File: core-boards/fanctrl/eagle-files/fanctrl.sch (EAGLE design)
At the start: 30 parts, among them J1 3-PIN_2MM-H, U1 MCP9701T-E/TT

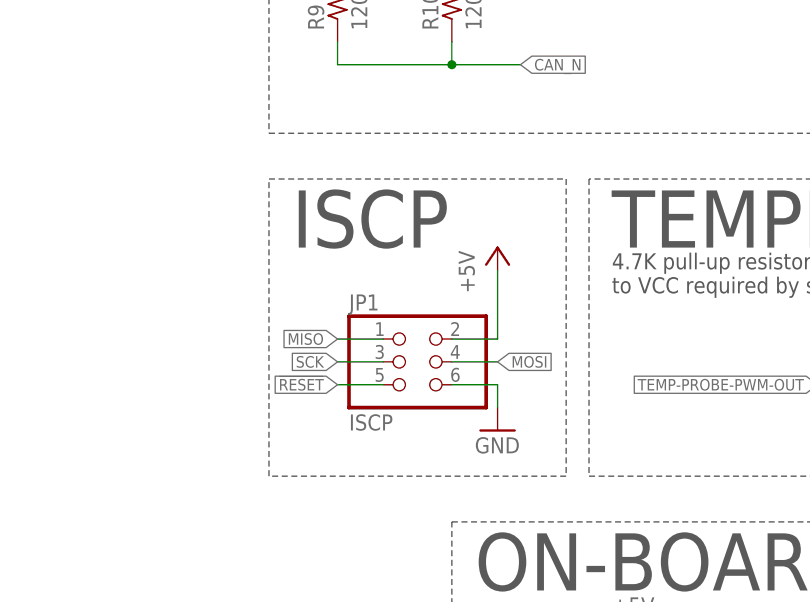
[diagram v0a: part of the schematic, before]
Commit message: Fix typo: ISCP --> ICSP.
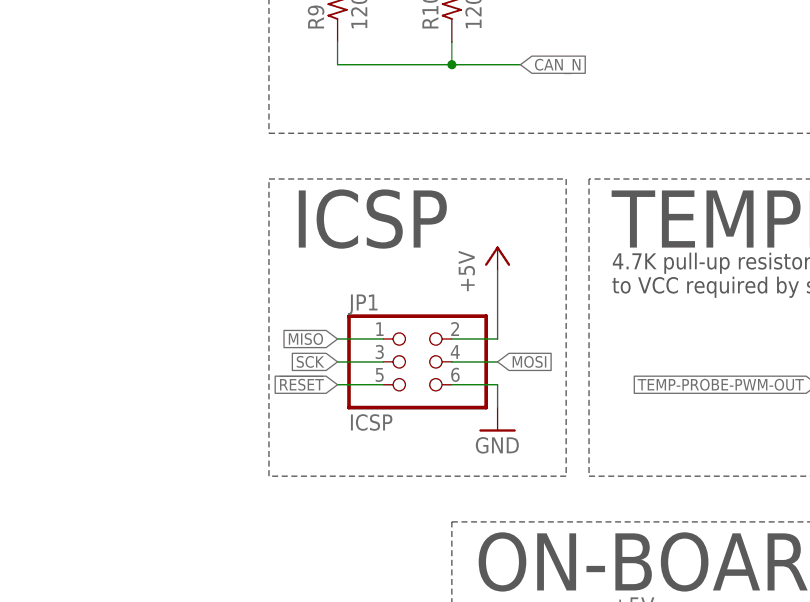
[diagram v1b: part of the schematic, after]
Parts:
- JP1: value ISCP -> ICSP
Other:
- note added: "ICSP"
- note removed: "ISCP"
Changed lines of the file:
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@@
 <part name="R9" library="rcl" library_urn="urn:adsk.eagle:library:334" deviceset="R-US_" device="R0603" package3d_urn="urn:adsk.eagle:package:23555/3" value="120Ω"/>
 <part name="R10" library="rcl" library_urn="urn:adsk.eagle:library:334" deviceset="R-US_" device="R0603" package3d_urn="urn:adsk.eagle:package:23555/3" value="120Ω"/>
-<part name="JP1" library="pinhead" library_urn="urn:adsk.eagle:library:325" deviceset="PINHD-2X3" device="" package3d_urn="urn:adsk.eagle:package:22462/2" value="ISCP"/>
+<part name="JP1" library="pinhead" library_urn="urn:adsk.eagle:library:325" deviceset="PINHD-2X3" device="" package3d_urn="urn:adsk.eagle:package:22462/2" value="ICSP"/>
 <part name="P+10" library="supply1" library_urn="urn:adsk.eagle:library:371" deviceset="+5V" device=""/>
 <part name="GND17" library="supply1" library_urn="urn:adsk.eagle:library:371" deviceset="GND" device=""/>
@@
 <wire x1="187.96" y1="129.54" x2="187.96" y2="96.52" width="0.1524" layer="97" style="shortdash"/>
 <wire x1="187.96" y1="96.52" x2="154.94" y2="96.52" width="0.1524" layer="97" style="shortdash"/>
-<text x="157.48" y="121.92" size="6.35" layer="97" font="vector" ratio="12">ISCP</text>
+<text x="157.48" y="121.92" size="6.35" layer="97" font="vector" ratio="12">ICSP</text>
 <text x="10.16" y="111.76" size="1.778" layer="97">IN = Write to the fan</text>
 <text x="10.16" y="109.22" size="1.778" layer="97">OUT = Read from the fan</text>

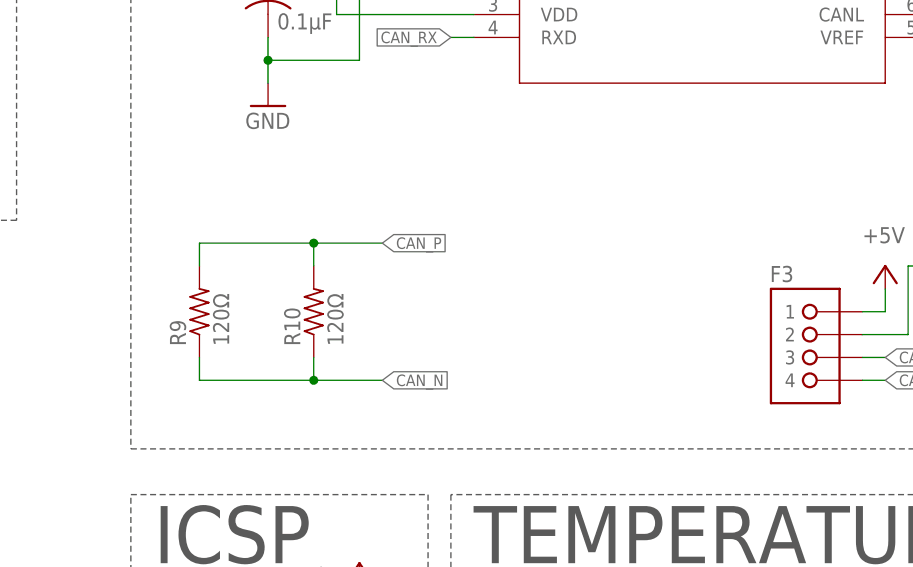
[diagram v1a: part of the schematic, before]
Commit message: Jank jumper for CAN resistor added.
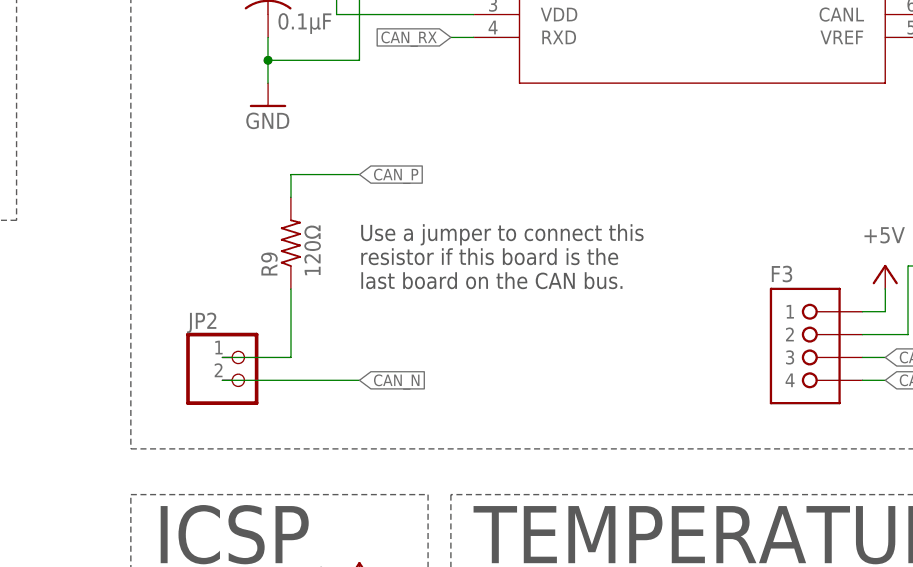
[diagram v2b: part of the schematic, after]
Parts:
- removed R10: 120Ω, rcl:R-US_R0603
- added JP2: (no value), pinhead:PINHD-1X2
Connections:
- new net N$1: JP2.1, R9.1
- net CAN_N: now also JP2.2; no longer R10.1, R9.1
- net CAN_P: no longer R10.2
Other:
- note added: "Use a jumper to connect this resistor if this board is the last board on the CAN bus."
- moved on the sheet: R9
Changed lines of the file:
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@@
 <part name="R8" library="rcl" library_urn="urn:adsk.eagle:library:334" deviceset="R-US_" device="R0603" package3d_urn="urn:adsk.eagle:package:23555/3" value="4.7K"/>
 <part name="R9" library="rcl" library_urn="urn:adsk.eagle:library:334" deviceset="R-US_" device="R0603" package3d_urn="urn:adsk.eagle:package:23555/3" value="120Ω"/>
-<part name="R10" library="rcl" library_urn="urn:adsk.eagle:library:334" deviceset="R-US_" device="R0603" package3d_urn="urn:adsk.eagle:package:23555/3" value="120Ω"/>
 <part name="JP1" library="pinhead" library_urn="urn:adsk.eagle:library:325" deviceset="PINHD-2X3" device="" package3d_urn="urn:adsk.eagle:package:22462/2" value="ICSP"/>
 <part name="P+10" library="supply1" library_urn="urn:adsk.eagle:library:371" deviceset="+5V" device=""/>
@@
 <part name="F3" library="RoboJackets-Connectors" deviceset="4-PIN_2MM-*" device="H"/>
 <part name="J1" library="RoboJackets-Connectors" deviceset="3-PIN_2MM-*" device="H"/>
+<part name="JP2" library="pinhead" library_urn="urn:adsk.eagle:library:325" deviceset="PINHD-1X2" device="" package3d_urn="urn:adsk.eagle:package:22435/2">
+<attribute name="SPICEPREFIX" value="B"/>
+</part>
 </parts>
 <sheets>
@@
 <text x="10.16" y="111.76" size="1.778" layer="97">IN = Write to the fan</text>
 <text x="10.16" y="109.22" size="1.778" layer="97">OUT = Read from the fan</text>
+<text x="180.34" y="152.4" size="1.778" layer="97" font="vector">Use a jumper to connect this
+resistor if this board is the
+last board on the CAN bus. </text>
 </plain>
 <instances>
@@
 <attribute name="VALUE" x="227.33" y="108.458" size="1.778" layer="96"/>
 </instance>
-<instance part="R9" gate="G$1" x="162.56" y="149.86" smashed="yes" rot="R90">
-<attribute name="NAME" x="161.0614" y="146.05" size="1.778" layer="95" rot="R90"/>
-<attribute name="VALUE" x="165.862" y="146.05" size="1.778" layer="96" rot="R90"/>
-</instance>
-<instance part="R10" gate="G$1" x="175.26" y="149.86" smashed="yes" rot="R90">
-<attribute name="NAME" x="173.7614" y="146.05" size="1.778" layer="95" rot="R90"/>
-<attribute name="VALUE" x="178.562" y="146.05" size="1.778" layer="96" rot="R90"/>
+<instance part="R9" gate="G$1" x="172.72" y="157.48" smashed="yes" rot="R90">
+<attribute name="NAME" x="171.2214" y="153.67" size="1.778" layer="95" rot="R90"/>
+<attribute name="VALUE" x="176.022" y="153.67" size="1.778" layer="96" rot="R90"/>
 </instance>
 <instance part="JP1" gate="A" x="170.18" y="109.22" smashed="yes">
@@
 <attribute name="NAME" x="248.92" y="119.38" size="1.778" layer="95" font="vector" align="top-left"/>
 <attribute name="VALUE" x="248.92" y="99.06" size="1.778" layer="96" font="vector"/>
+</instance>
+<instance part="JP2" gate="G$1" x="167.64" y="142.24" smashed="yes">
+<attribute name="NAME" x="161.29" y="147.955" size="1.778" layer="95"/>
+<attribute name="VALUE" x="161.29" y="137.16" size="1.778" layer="96"/>
 </instance>
 </instances>
@@
 </segment>
 <segment>
-<pinref part="R10" gate="G$1" pin="2"/>
-<label x="182.88" y="157.48" size="1.27" layer="95" font="vector" xref="yes"/>
+<wire x1="172.72" y1="165.1" x2="180.34" y2="165.1" width="0.1524" layer="91"/>
+<label x="180.34" y="165.1" size="1.27" layer="95" font="vector" xref="yes"/>
 <pinref part="R9" gate="G$1" pin="2"/>
-<wire x1="162.56" y1="154.94" x2="162.56" y2="157.48" width="0.1524" layer="91"/>
-<wire x1="162.56" y1="157.48" x2="175.26" y2="157.48" width="0.1524" layer="91"/>
-<wire x1="175.26" y1="157.48" x2="175.26" y2="154.94" width="0.1524" layer="91"/>
-<wire x1="175.26" y1="157.48" x2="182.88" y2="157.48" width="0.1524" layer="91"/>
-<junction x="175.26" y="157.48"/>
+<wire x1="172.72" y1="165.1" x2="172.72" y2="162.56" width="0.1524" layer="91"/>
 </segment>
 </net>
@@
 </segment>
 <segment>
-<pinref part="R10" gate="G$1" pin="1"/>
-<label x="182.88" y="142.24" size="1.27" layer="95" font="vector" xref="yes"/>
-<pinref part="R9" gate="G$1" pin="1"/>
-<wire x1="162.56" y1="144.78" x2="162.56" y2="142.24" width="0.1524" layer="91"/>
-<wire x1="162.56" y1="142.24" x2="175.26" y2="142.24" width="0.1524" layer="91"/>
-<wire x1="175.26" y1="142.24" x2="182.88" y2="142.24" width="0.1524" layer="91"/>
-<wire x1="175.26" y1="144.78" x2="175.26" y2="142.24" width="0.1524" layer="91"/>
-<junction x="175.26" y="142.24"/>
+<pinref part="JP2" gate="G$1" pin="2"/>
+<wire x1="165.1" y1="142.24" x2="180.34" y2="142.24" width="0.1524" layer="91"/>
+<label x="180.34" y="142.24" size="1.27" layer="95" font="vector" xref="yes"/>
 </segment>
 </net>
@@
 </segment>
 </net>
+<net name="N$1" class="0">
+<segment>
+<pinref part="JP2" gate="G$1" pin="1"/>
+<wire x1="165.1" y1="144.78" x2="172.72" y2="144.78" width="0.1524" layer="91"/>
+<pinref part="R9" gate="G$1" pin="1"/>
+<wire x1="172.72" y1="144.78" x2="172.72" y2="152.4" width="0.1524" layer="91"/>
+</segment>
+</net>

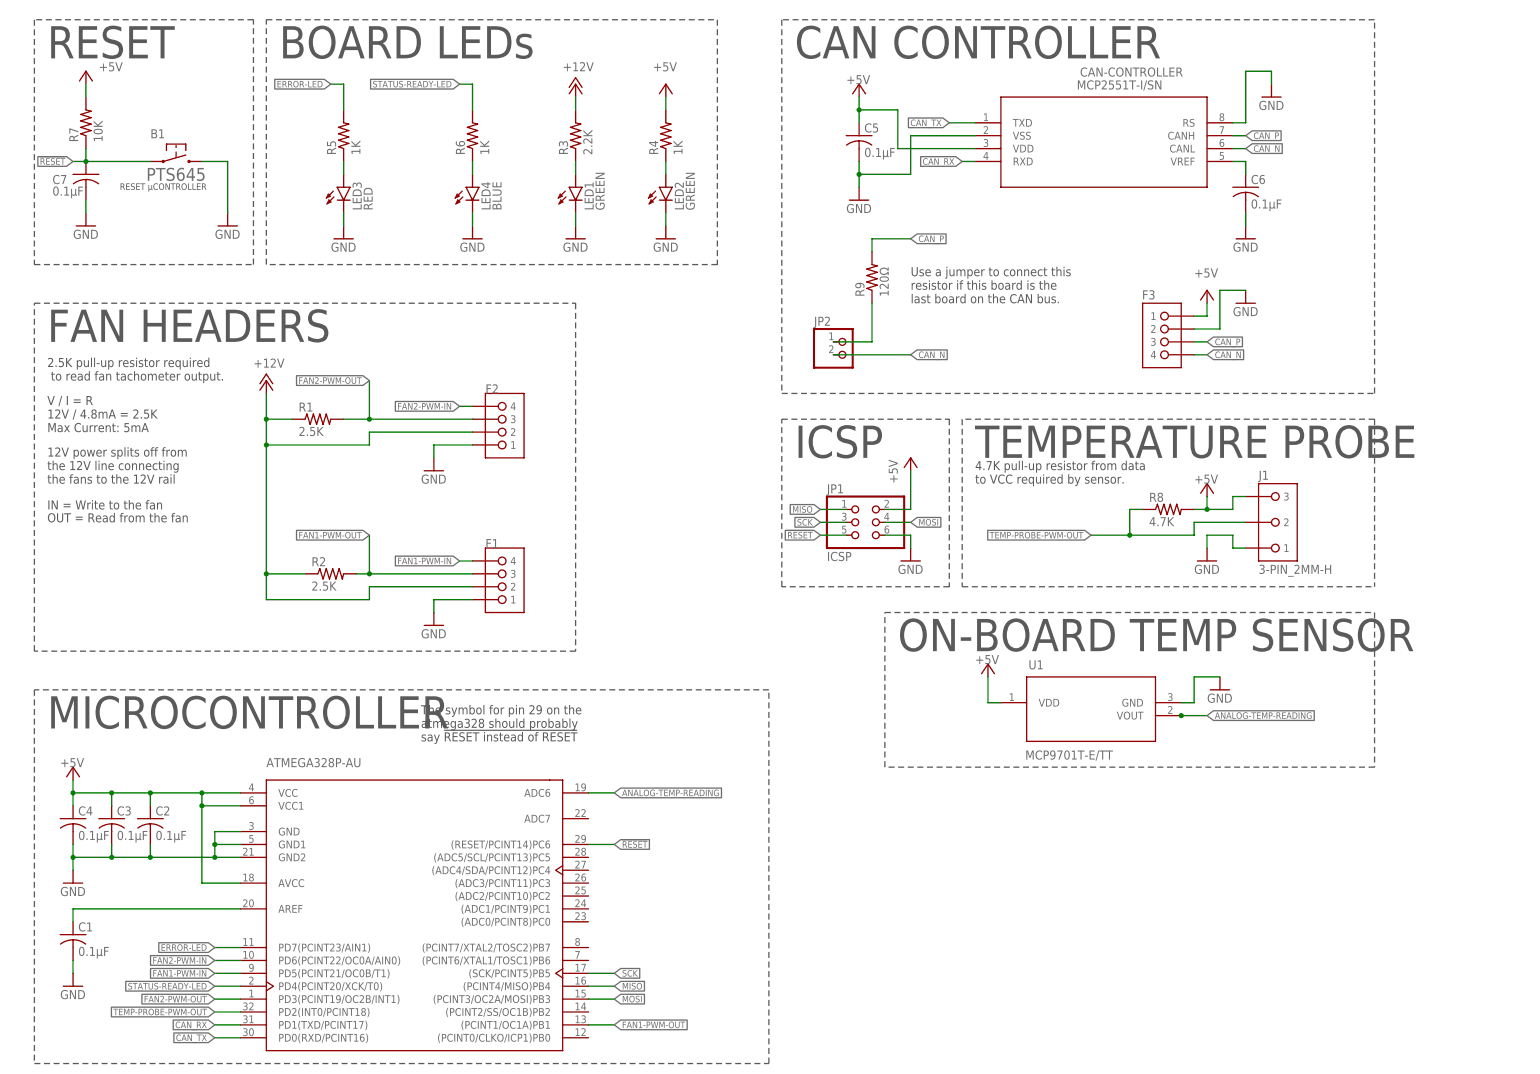
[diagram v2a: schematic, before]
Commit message: Fix LED Resist. values --> 470ohm
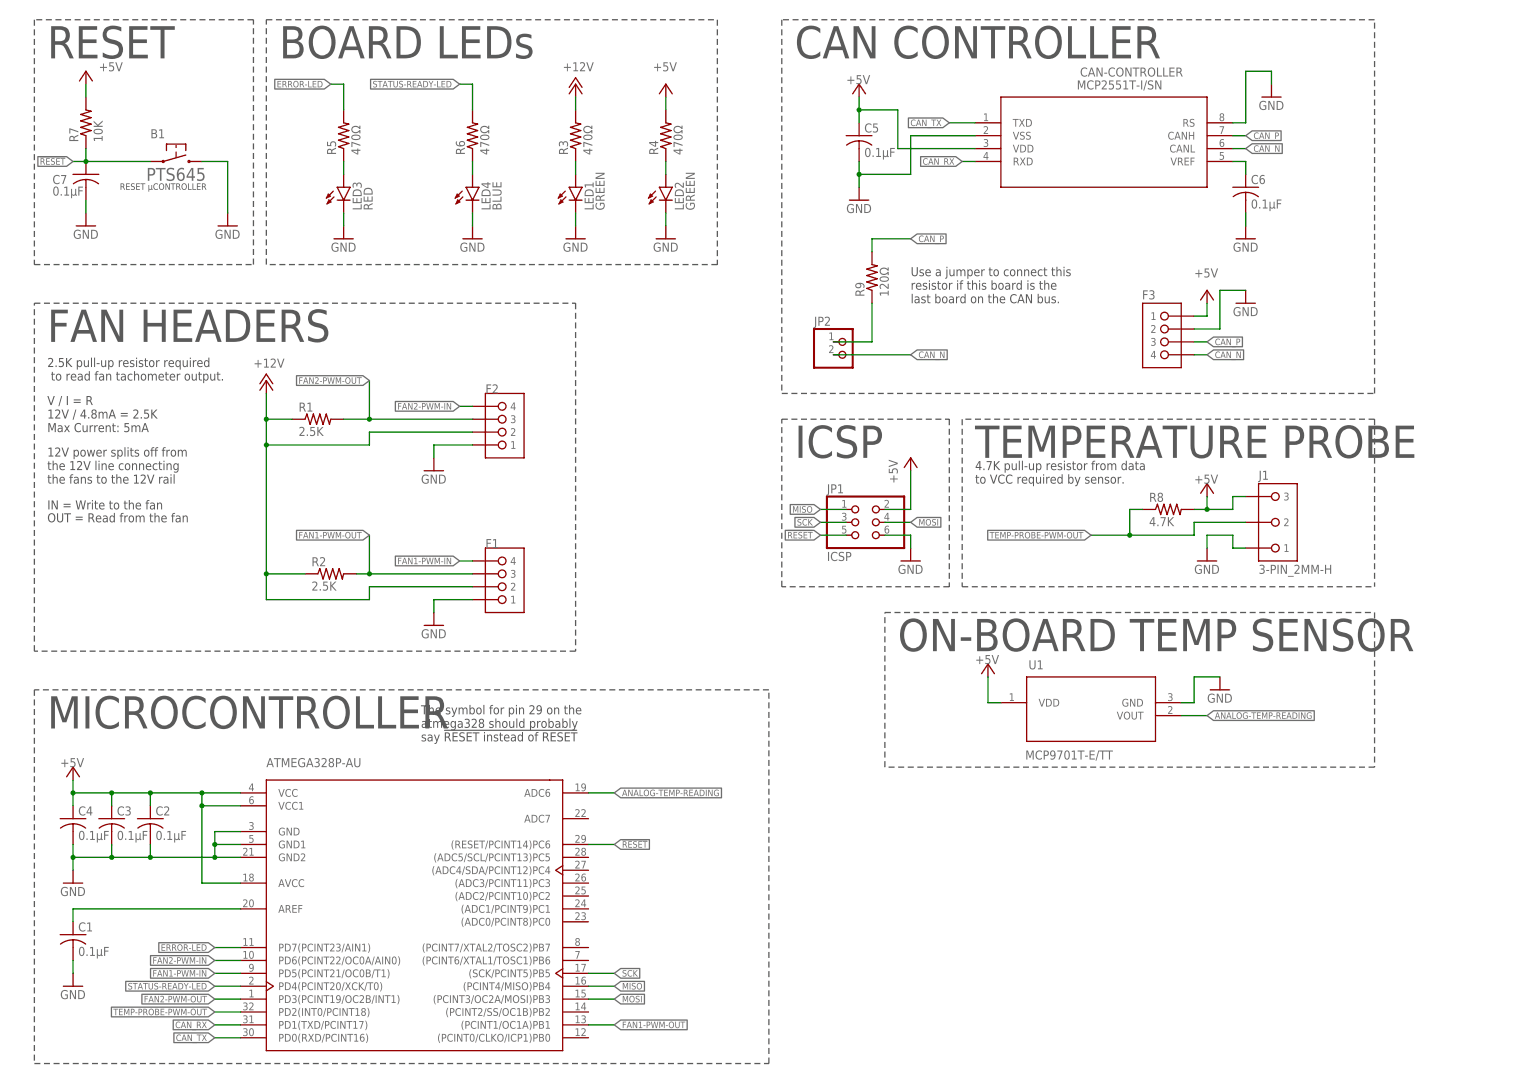
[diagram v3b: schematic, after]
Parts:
- R3: value 2.2K -> 470Ω
- R4, R5, R6: value 1K -> 470Ω
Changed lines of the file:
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@@
 <part name="C4" library="rcl" library_urn="urn:adsk.eagle:library:334" deviceset="C-US" device="C0603" package3d_urn="urn:adsk.eagle:package:23616/2" value="0.1µF"/>
 <part name="GND1" library="supply1" library_urn="urn:adsk.eagle:library:371" deviceset="GND" device=""/>
-<part name="R3" library="rcl" library_urn="urn:adsk.eagle:library:334" deviceset="R-US_" device="R0603" package3d_urn="urn:adsk.eagle:package:23555/3" value="2.2K"/>
-<part name="R4" library="rcl" library_urn="urn:adsk.eagle:library:334" deviceset="R-US_" device="R0603" package3d_urn="urn:adsk.eagle:package:23555/3" value="1K"/>
+<part name="R3" library="rcl" library_urn="urn:adsk.eagle:library:334" deviceset="R-US_" device="R0603" package3d_urn="urn:adsk.eagle:package:23555/3" value="470Ω"/>
+<part name="R4" library="rcl" library_urn="urn:adsk.eagle:library:334" deviceset="R-US_" device="R0603" package3d_urn="urn:adsk.eagle:package:23555/3" value="470Ω"/>
 <part name="LED1" library="led" library_urn="urn:adsk.eagle:library:259" deviceset="LED" device="CHIPLED_0603" package3d_urn="urn:adsk.eagle:package:15822/2" value="GREEN"/>
 <part name="P+1" library="supply1" library_urn="urn:adsk.eagle:library:371" deviceset="+12V" device=""/>
@@
 <part name="GND8" library="supply1" library_urn="urn:adsk.eagle:library:371" deviceset="GND" device=""/>
 <part name="LED2" library="led" library_urn="urn:adsk.eagle:library:259" deviceset="LED" device="CHIPLED_0603" package3d_urn="urn:adsk.eagle:package:15822/2" value="GREEN"/>
-<part name="R5" library="rcl" library_urn="urn:adsk.eagle:library:334" deviceset="R-US_" device="R0603" package3d_urn="urn:adsk.eagle:package:23555/3" value="1K"/>
+<part name="R5" library="rcl" library_urn="urn:adsk.eagle:library:334" deviceset="R-US_" device="R0603" package3d_urn="urn:adsk.eagle:package:23555/3" value="470Ω"/>
 <part name="GND9" library="supply1" library_urn="urn:adsk.eagle:library:371" deviceset="GND" device=""/>
 <part name="LED3" library="led" library_urn="urn:adsk.eagle:library:259" deviceset="LED" device="CHIPLED_0603" package3d_urn="urn:adsk.eagle:package:15822/2" value="RED"/>
-<part name="R6" library="rcl" library_urn="urn:adsk.eagle:library:334" deviceset="R-US_" device="R0603" package3d_urn="urn:adsk.eagle:package:23555/3" value="1K"/>
+<part name="R6" library="rcl" library_urn="urn:adsk.eagle:library:334" deviceset="R-US_" device="R0603" package3d_urn="urn:adsk.eagle:package:23555/3" value="470Ω"/>
 <part name="GND10" library="supply1" library_urn="urn:adsk.eagle:library:371" deviceset="GND" device=""/>
 <part name="LED4" library="led" library_urn="urn:adsk.eagle:library:259" deviceset="LED" device="CHIPLED_0603" package3d_urn="urn:adsk.eagle:package:15822/2" value="BLUE"/>
@@
 <wire x1="233.68" y1="71.12" x2="238.76" y2="71.12" width="0.1524" layer="91"/>
 <pinref part="U1" gate="MCP9701" pin="VOUT"/>
-<junction x="233.68" y="71.12"/>
-</segment>
-<segment>
+</segment>
+<segment>
